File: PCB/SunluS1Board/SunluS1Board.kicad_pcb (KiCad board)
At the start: 2 copper layers, 48.2 x 57 mm, 45 parts, among them J1 Conn_01x14, J2 aNTC, J3 hNTC, J4 Fan, J5 HT, J6 Power, J7 Conn_02x03_Odd_Even, Q1 SIA440DJ-T1-GE3, Q2 AO3400A, Q3 AO3400A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

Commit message: continue routing
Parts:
- moved Q2 0.70 mm to (81.4, 64.4)
- renumbered J4 to FAN, J5 to HT, J6 to Vin, J2 to aNTC, J3 to hNTC
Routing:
- net +24V: track 18.6 -> 56.9 mm
- net Net-(Q2-G): track 0.00 -> 6.04 mm
- net Led: track 0.00 -> 3.97 mm
- net Net-(D1-K): track 0.00 -> 1.95 mm
- net fCon: track 7.49 -> 8.70 mm
- net GND: track 34.6 -> 34.9 mm, vias 7 -> 31
- added copper zone on B.Cu, net GND
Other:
- outline, holes or cut-outs redrawn

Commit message: DRC and 3d models
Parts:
- renumbered aNTC to J2, hNTC to J3, FAN to J4, HT to J5, Vin to J6
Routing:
- net GND: track 34.9 -> 40.4 mm

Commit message: fixes
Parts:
- J7: footprint Connector_PinSocket_2.54mm:PinSocket_2x03_P2.54mm_Vertical_SMD -> Connector_PinHeader_2.54mm:PinHeader_2x03_P2.54mm_Vertical_SMD
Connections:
- J7 pad 1: NRST -> GND
- J7 pad 2: GND -> NRST
- J7 pad 3: SWCLK -> GND
- J7 pad 4: GND -> SWCLK
- J7 pad 5: SWDIO -> +3.3V
- J7 pad 6: +3.3V -> SWDIO
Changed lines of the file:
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@@
 		)
 	)
-	(footprint "Connector_PinSocket_2.54mm:PinSocket_2x03_P2.54mm_Vertical_SMD"
+	(footprint "Connector_PinHeader_2.54mm:PinHeader_2x03_P2.54mm_Vertical_SMD"
 		(layer "F.Cu")
 		(at 93.78 41.36)
-		(descr "surface-mounted straight socket strip, 2x03, 2.54mm pitch, double cols (from Kicad 4.0.7), script generated")
-		(tags "Surface mounted socket strip SMD 2x03 2.54mm double row")
+		(descr "surface-mounted straight pin header, 2x03, 2.54mm pitch, double rows")
+		(tags "Surface mounted pin header SMD 2x03 2.54mm double row")
 		(property "Reference" "J7"
-			(at 0 -5.31 0)
+			(at 0 -4.92 0)
 			(layer "F.SilkS")
 			(effects
@@
 		)
 		(property "Value" "Conn_02x03_Odd_Even"
-			(at 0 5.31 0)
+			(at 0 4.92 0)
 			(layer "F.Fab")
 			(effects
@@
 		(attr smd)
 		(fp_line
-			(start -2.6 -3.87)
-			(end -2.6 -3.3)
+			(start -4.04 -3.35)
+			(end -2.65 -3.35)
 			(stroke
 				(width 0.12)
@@
 		)
 		(fp_line
-			(start -2.6 -3.87)
-			(end 2.6 -3.87)
+			(start -2.65 -3.92)
+			(end -2.65 -3.35)
 			(stroke
 				(width 0.12)
@@
 		)
 		(fp_line
-			(start -2.6 -1.78)
-			(end -2.6 -0.76)
+			(start -2.65 -3.92)
+			(end 2.65 -3.92)
 			(stroke
 				(width 0.12)
@@
 		)
 		(fp_line
-			(start -2.6 0.76)
-			(end -2.6 1.78)
+			(start -2.65 -1.73)
+			(end -2.65 -0.81)
 			(stroke
 				(width 0.12)
@@
 		)
 		(fp_line
-			(start -2.6 3.3)
-			(end -2.6 3.87)
+			(start -2.65 0.81)
+			(end -2.65 1.73)
 			(stroke
 				(width 0.12)
@@
 		)
 		(fp_line
-			(start -2.6 3.87)
-			(end 2.6 3.87)
+			(start -2.65 3.35)
+			(end -2.65 3.92)
 			(stroke
 				(width 0.12)
@@
 		)
 		(fp_line
-			(start 2.6 -3.87)
-			(end 2.6 -3.3)
+			(start -2.65 3.92)
+			(end 2.65 3.92)
 			(stroke
 				(width 0.12)
@@
 		)
 		(fp_line
-			(start 2.6 -3.3)
-			(end 3.96 -3.3)
+			(start 2.65 -3.92)
+			(end 2.65 -3.35)
 			(stroke
 				(width 0.12)
@@
 		)
 		(fp_line
-			(start 2.6 -1.78)
-			(end 2.6 -0.76)
+			(start 2.65 -1.73)
+			(end 2.65 -0.81)
 			(stroke
 				(width 0.12)
@@
 		)
 		(fp_line
-			(start 2.6 0.76)
-			(end 2.6 1.78)
+			(start 2.65 0.81)
+			(end 2.65 1.73)
 			(stroke
 				(width 0.12)
@@
 		)
 		(fp_line
-			(start 2.6 3.3)
-			(end 2.6 3.87)
+			(start 2.65 3.35)
+			(end 2.65 3.92)
 			(stroke
 				(width 0.12)
@@
 		)
 		(fp_line
-			(start -4.55 -4.35)
-			(end 4.5 -4.35)
+			(start -5.87 -4.31)
+			(end -5.87 4.31)
 			(stroke
 				(width 0.05)
@@
 		)
 		(fp_line
-			(start -4.55 4.3)
-			(end -4.55 -4.35)
+			(start -5.87 4.31)
+			(end 5.88 4.31)
 			(stroke
 				(width 0.05)
@@
 		)
 		(fp_line
-			(start 4.5 -4.35)
-			(end 4.5 4.3)
+			(start 5.88 -4.31)
+			(end -5.87 -4.31)
 			(stroke
 				(width 0.05)
@@
 		)
 		(fp_line
-			(start 4.5 4.3)
-			(end -4.55 4.3)
+			(start 5.88 4.31)
+			(end 5.88 -4.31)
 			(stroke
 				(width 0.05)
@@
 		)
 		(fp_line
-			(start -3.92 -2.86)
-			(end -2.54 -2.86)
+			(start -3.6 -2.86)
+			(end -3.6 -2.22)
 			(stroke
 				(width 0.1)
@@
 		)
 		(fp_line
-			(start -3.92 -2.22)
-			(end -3.92 -2.86)
+			(start -3.6 -2.22)
+			(end -2.54 -2.22)
 			(stroke
 				(width 0.1)
@@
 		)
 		(fp_line
-			(start -3.92 -0.32)
-			(end -2.54 -0.32)
+			(start -3.6 -0.32)
+			(end -3.6 0.32)
 			(stroke
 				(width 0.1)
@@
 		)
 		(fp_line
-			(start -3.92 0.32)
-			(end -3.92 -0.32)
+			(start -3.6 0.32)
+			(end -2.54 0.32)
 			(stroke
 				(width 0.1)
@@
 		)
 		(fp_line
-			(start -3.92 2.22)
-			(end -2.54 2.22)
+			(start -3.6 2.22)
+			(end -3.6 2.86)
 			(stroke
 				(width 0.1)
@@
 		)
 		(fp_line
-			(start -3.92 2.86)
-			(end -3.92 2.22)
+			(start -3.6 2.86)
+			(end -2.54 2.86)
 			(stroke
 				(width 0.1)
@@
 		)
 		(fp_line
-			(start -2.54 -3.81)
-			(end 1.54 -3.81)
+			(start -2.54 -2.86)
+			(end -3.6 -2.86)
 			(stroke
 				(width 0.1)
@@
 		)
 		(fp_line
-			(start -2.54 -2.22)
-			(end -3.92 -2.22)
+			(start -2.54 -2.86)
+			(end -1.59 -3.81)
 			(stroke
 				(width 0.1)
@@
 		)
 		(fp_line
-			(start -2.54 0.32)
-			(end -3.92 0.32)
+			(start -2.54 -0.32)
+			(end -3.6 -0.32)
 			(stroke
 				(width 0.1)
@@
 		)
 		(fp_line
-			(start -2.54 2.86)
-			(end -3.92 2.86)
+			(start -2.54 2.22)
+			(end -3.6 2.22)
 			(stroke
 				(width 0.1)
@@
 		(fp_line
 			(start -2.54 3.81)
-			(end -2.54 -3.81)
+			(end -2.54 -2.86)
 			(stroke
 				(width 0.1)
@@
 		)
 		(fp_line
-			(start 1.54 -3.81)
-			(end 2.54 -2.81)
+			(start -1.59 -3.81)
+			(end 2.54 -3.81)
 			(stroke
 				(width 0.1)
@@
 		)
 		(fp_line
-			(start 2.54 -2.86)
-			(end 3.92 -2.86)
+			(start 2.54 -3.81)
+			(end 2.54 3.81)
 			(stroke
 				(width 0.1)
@@
 		)
 		(fp_line
-			(start 2.54 -2.81)
-			(end 2.54 3.81)
+			(start 2.54 -2.86)
+			(end 3.6 -2.86)
 			(stroke
 				(width 0.1)
@@
 		(fp_line
 			(start 2.54 -0.32)
-			(end 3.92 -0.32)
+			(end 3.6 -0.32)
 			(stroke
 				(width 0.1)
@@
 		(fp_line
 			(start 2.54 2.22)
-			(end 3.92 2.22)
+			(end 3.6 2.22)
 			(stroke
 				(width 0.1)
@@
 		)
 		(fp_line
-			(start 3.92 -2.86)
-			(end 3.92 -2.22)
+			(start 3.6 -2.86)
+			(end 3.6 -2.22)
 			(stroke
 				(width 0.1)
@@
 		)
 		(fp_line
-			(start 3.92 -2.22)
+			(start 3.6 -2.22)
 			(end 2.54 -2.22)
 			(stroke
@@
 		)
 		(fp_line
-			(start 3.92 -0.32)
-			(end 3.92 0.32)
+			(start 3.6 -0.32)
+			(end 3.6 0.32)
 			(stroke
 				(width 0.1)
@@
 		)
 		(fp_line
-			(start 3.92 0.32)
+			(start 3.6 0.32)
 			(end 2.54 0.32)
 			(stroke
@@
 		)
 		(fp_line
-			(start 3.92 2.22)
-			(end 3.92 2.86)
+			(start 3.6 2.22)
+			(end 3.6 2.86)
 			(stroke
 				(width 0.1)
@@
 		)
 		(fp_line
-			(start 3.92 2.86)
+			(start 3.6 2.86)
 			(end 2.54 2.86)
 			(stroke
@@
 		)
 		(pad "1" smd rect
-			(at 2.52 -2.54)
-			(size 3 1)
+			(at -2.525 -2.54)
+			(size 3.15 1)
 			(layers "F.Cu" "F.Mask" "F.Paste")
-			(net 22 "NRST")
+			(net 1 "GND")
 			(pinfunction "Pin_1")
 			(pintype "passive")
 		)
 		(pad "2" smd rect
-			(at -2.52 -2.54)
-			(size 3 1)
+			(at 2.525 -2.54)
+			(size 3.15 1)
 			(layers "F.Cu" "F.Mask" "F.Paste")
-			(net 1 "GND")
+			(net 22 "NRST")
 			(pinfunction "Pin_2")
 			(pintype "passive")
 		)
 		(pad "3" smd rect
-			(at 2.52 0)
-			(size 3 1)
+			(at -2.525 0)
+			(size 3.15 1)
 			(layers "F.Cu" "F.Mask" "F.Paste")
-			(net 24 "SWCLK")
+			(net 1 "GND")
 			(pinfunction "Pin_3")
 			(pintype "passive")
 		)
 		(pad "4" smd rect
-			(at -2.52 0)
-			(size 3 1)
+			(at 2.525 0)
+			(size 3.15 1)
 			(layers "F.Cu" "F.Mask" "F.Paste")
-			(net 1 "GND")
+			(net 24 "SWCLK")
 			(pinfunction "Pin_4")
 			(pintype "passive")
 		)
 		(pad "5" smd rect
-			(at 2.52 2.54)
-			(size 3 1)
+			(at -2.525 2.54)
+			(size 3.15 1)
 			(layers "F.Cu" "F.Mask" "F.Paste")
-			(net 23 "SWDIO")
+			(net 4 "+3.3V")
 			(pinfunction "Pin_5")
 			(pintype "passive")
 		)
 		(pad "6" smd rect
-			(at -2.52 2.54)
-			(size 3 1)
+			(at 2.525 2.54)
+			(size 3.15 1)
 			(layers "F.Cu" "F.Mask" "F.Paste")
-			(net 4 "+3.3V")
+			(net 23 "SWDIO")
 			(pinfunction "Pin_6")
 			(pintype "passive")
 		)
 		(embedded_fonts no)
-		(model "${KICAD9_3DMODEL_DIR}/Connector_PinSocket_2.54mm.3dshapes/PinSocket_2x03_P2.54mm_Vertical_SMD.step"
+		(model "${KICAD9_3DMODEL_DIR}/Connector_PinHeader_2.54mm.3dshapes/PinHeader_2x03_P2.54mm_Vertical_SMD.step"
 			(offset
 				(xyz 0 0 0)
@@
 		(at 75.5 68.1)
 		(property "Reference" "SW2"
-			(at 0 4 180)
+			(at 0 -2.9 180)
 			(layer "B.SilkS")
 			(effects
@@
 		(at 97.82 68.1)
 		(property "Reference" "SW1"
-			(at 0 4 180)
+			(at 0 -3.1 180)
 			(layer "B.SilkS")
 			(effects

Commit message: schematic
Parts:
- moved SW2 2.20 mm to (73.3, 68.1)
- moved SW1 2.20 mm to (95.6, 68.1)
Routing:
- net GND: track 40.4 -> 42.8 mm
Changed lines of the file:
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@@
 	(footprint "easyeda2kicad:SW-SMD_L3.9-W3.0-P4.45"
 		(layer "B.Cu")
-		(at 75.5 68.1)
+		(at 73.3 68.1)
 		(property "Reference" "SW2"
 			(at 0 -2.9 180)
@@
 	(footprint "easyeda2kicad:SW-SMD_L3.9-W3.0-P4.45"
 		(layer "B.Cu")
-		(at 97.82 68.1)
+		(at 95.62 68.1)
 		(property "Reference" "SW1"
 			(at 0 -3.1 180)
@@
 	)
 	(via
-		(at 94.4 68.1)
+		(at 95.2 68.1)
 		(size 0.6)
 		(drill 0.3)
@@
 	)
 	(segment
-		(start 95.64 68.1)
-		(end 94.4 68.1)
+		(start 75.401 41.701)
+		(end 79.299 41.701)
+		(width 0.2)
+		(layer "B.Cu")
+		(net 1)
+	)
+	(segment
+		(start 78.5 42.5)
+		(end 78.5 49)
+		(width 0.2)
+		(layer "B.Cu")
+		(net 1)
+	)
+	(segment
+		(start 73.8 47.8)
+		(end 75 49)
+		(width 0.2)
+		(layer "B.Cu")
+		(net 1)
+	)
+	(segment
+		(start 79.299 41.701)
+		(end 79.5 41.5)
+		(width 0.2)
+		(layer "B.Cu")
+		(net 1)
+	)
+	(segment
+		(start 75 49)
+		(end 75.5 49)
+		(width 0.2)
+		(layer "B.Cu")
+		(net 1)
+	)
+	(segment
+		(start 73.32 68.72)
+		(end 71.74 68.72)
+		(width 0.8)
+		(layer "B.Cu")
+		(net 1)
+	)
+	(segment
+		(start 71.74 68.72)
+		(end 71.12 68.1)
+		(width 0.8)
+		(layer "B.Cu")
+		(net 1)
+	)
+	(segment
+		(start 93.44 68.1)
+		(end 95.2 68.1)
 		(width 0.8)
 		(layer "B.Cu")
@@
 	)
 	(segment
-		(start 75.401 41.701)
-		(end 79.299 41.701)
-		(width 0.2)
-		(layer "B.Cu")
-		(net 1)
-	)
-	(segment
-		(start 78.5 42.5)
-		(end 78.5 49)
-		(width 0.2)
-		(layer "B.Cu")
-		(net 1)
-	)
-	(segment
-		(start 73.8 47.8)
-		(end 75 49)
-		(width 0.2)
-		(layer "B.Cu")
-		(net 1)
-	)
-	(segment
-		(start 79.299 41.701)
-		(end 79.5 41.5)
-		(width 0.2)
-		(layer "B.Cu")
-		(net 1)
-	)
-	(segment
-		(start 75 49)
-		(end 75.5 49)
-		(width 0.2)
-		(layer "B.Cu")
-		(net 1)
-	)
-	(segment
 		(start 74 69.4)
 		(end 73.32 68.72)
@@
 		(layer "B.Cu")
 		(net 1)
-	)
-	(segment
-		(start 73.32 68.72)
-		(end 73.32 68.1)
-		(width 0.8)
-		(layer "B.Cu")
-		(net 1)

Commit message: continue buck
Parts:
- removed C5, C7: 100nF, Capacitor_SMD:C_0603_1608Metric
- removed C6, C8: 1uF, Capacitor_SMD:C_0805_2012Metric
- removed D3: 1N4007W, Diode_SMD:Nexperia_CFP3_SOD-123W
- removed U2: AP7381-33SA-7, Package_TO_SOT_SMD:SOT-23
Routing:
- net +24V: track 56.9 -> 48.2 mm
- net +3.3V: track 37.6 -> 34.6 mm, vias 9 -> 7
- net Net-(D3-K): track 2.87 -> 0.00 mm

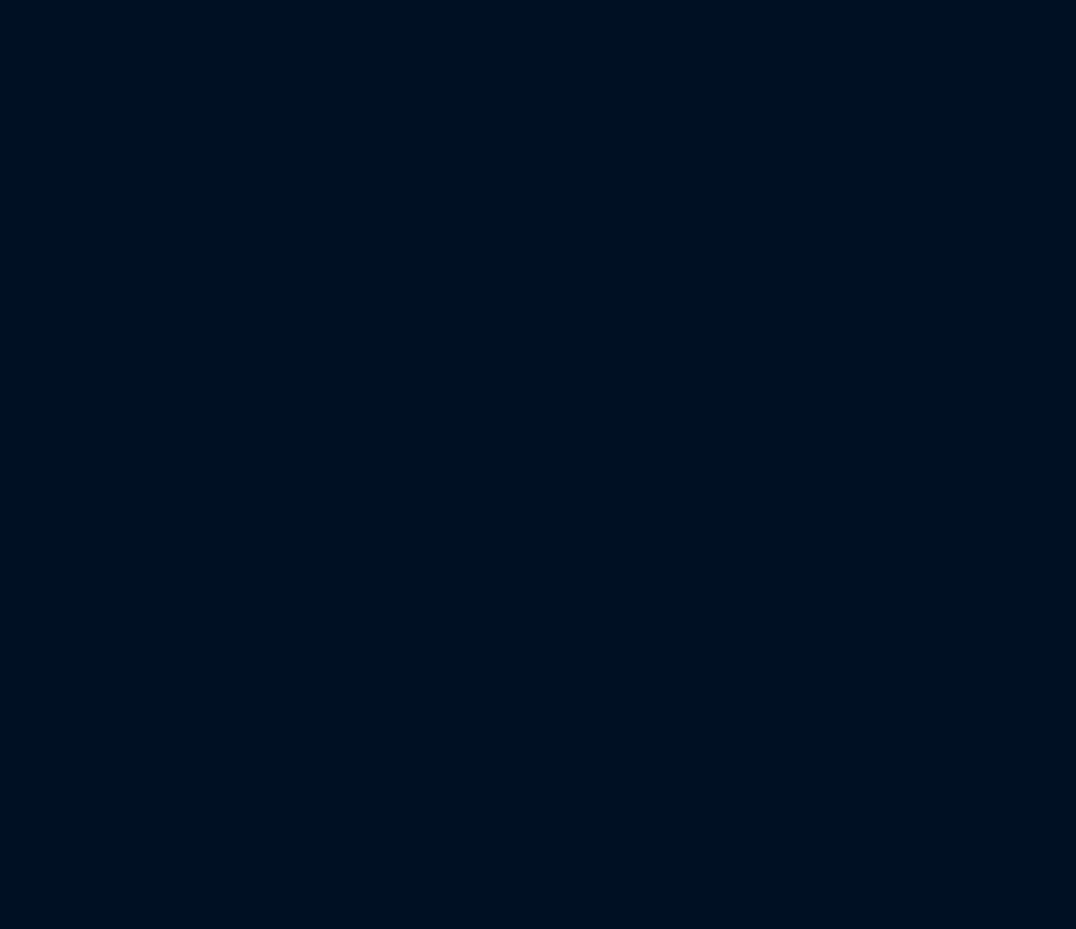
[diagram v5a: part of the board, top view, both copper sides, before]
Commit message: start buck pcb
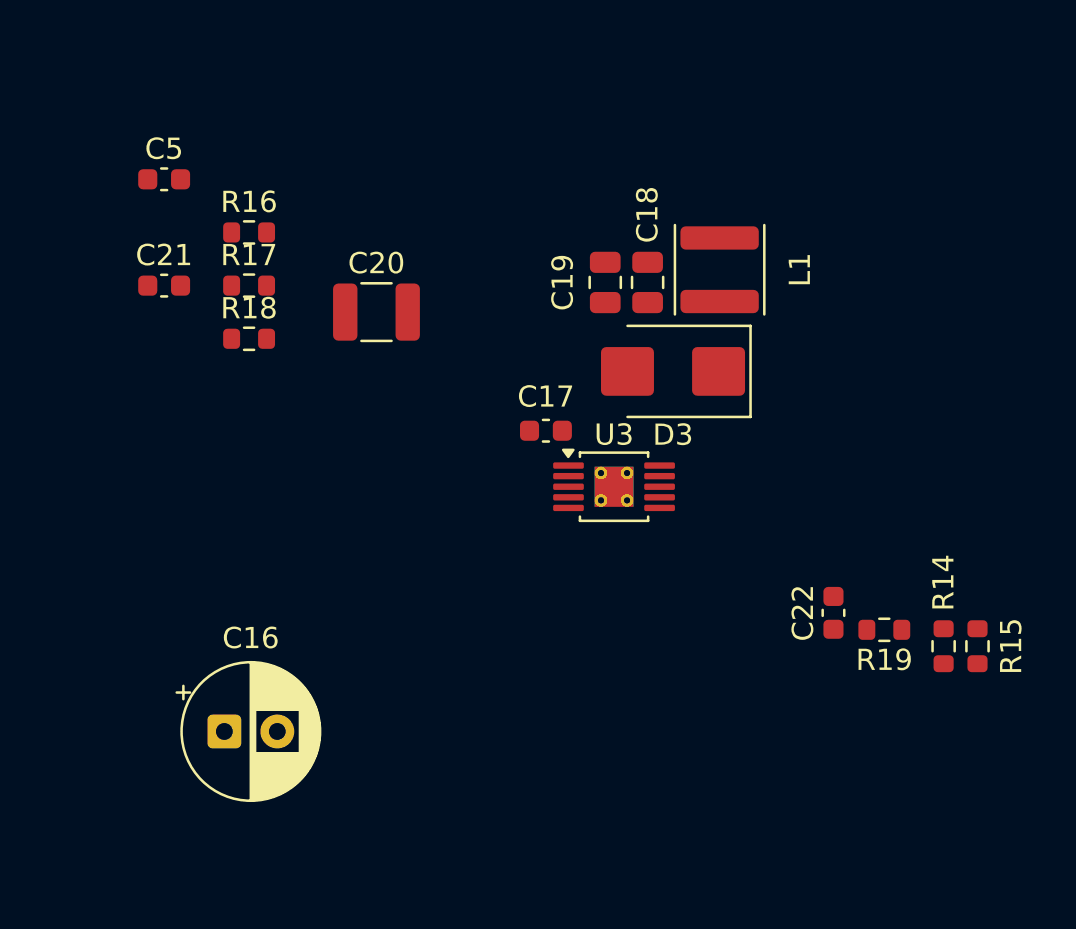
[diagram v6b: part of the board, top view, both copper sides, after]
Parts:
- added C16: 100uF, Capacitor_THT:CP_Radial_D6.3mm_P2.50mm, F.Cu at (125.6, 64.8)
- added C17: 0.1uF, Capacitor_SMD:C_0603_1608Metric, F.Cu at (140.8, 50.6)
- added C18: 22uF, Capacitor_SMD:C_0805_2012Metric, F.Cu at (145.6, 43.6)
- added C19: 22uF, Capacitor_SMD:C_0805_2012Metric, F.Cu at (143.6, 43.6)
- added C20: 10uF, Capacitor_SMD:C_1210_3225Metric, F.Cu at (132.8, 45.0)
- added C21: 10nF, Capacitor_SMD:C_0603_1608Metric, F.Cu at (122.8, 43.8)
- added C22: 4.7nF, Capacitor_SMD:C_0603_1608Metric, F.Cu at (154.4, 59.2)
- added C5: 0.1uF, Capacitor_SMD:C_0603_1608Metric, F.Cu at (122.8, 38.7)
- added D3: B360, Diode_SMD:D_SMB, F.Cu at (146.8, 47.8)
- added L1: 10uH, Inductor_SMD:L_APV_ANR4020, F.Cu at (149.0, 43.0)
- added R14: 31.6k, Resistor_SMD:R_0603_1608Metric, F.Cu at (159.6, 60.8)
- added R15: 10k, Resistor_SMD:R_0603_1608Metric, F.Cu at (161.2, 60.8)
- added R16: 124k, Resistor_SMD:R_0603_1608Metric, F.Cu at (126.8, 41.2)
- added R17: 30.1k, Resistor_SMD:R_0603_1608Metric, F.Cu at (126.8, 43.8)
- added R18: 412k, Resistor_SMD:R_0603_1608Metric, F.Cu at (126.8, 46.3)
- added R19: 20k, Resistor_SMD:R_0603_1608Metric, F.Cu at (156.8, 60.0)
- added U3: TPS54240DGQ, Package_SO:HVSSOP-10-1EP_3x3mm_P0.5mm_EP1.83x1.89mm_ThermalVias, F.Cu at (144.0, 53.2)

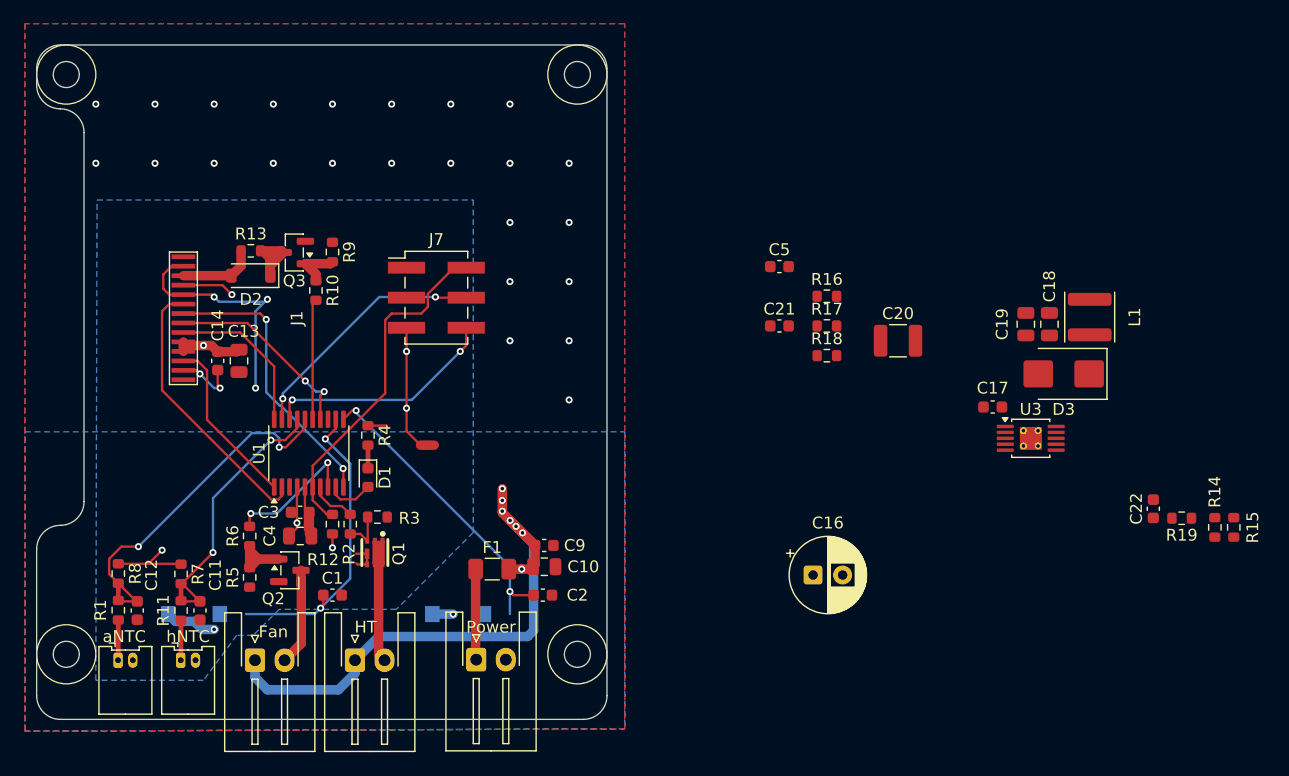
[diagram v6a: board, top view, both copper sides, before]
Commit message: f*** I placed and routed the buck at the wrong layer...
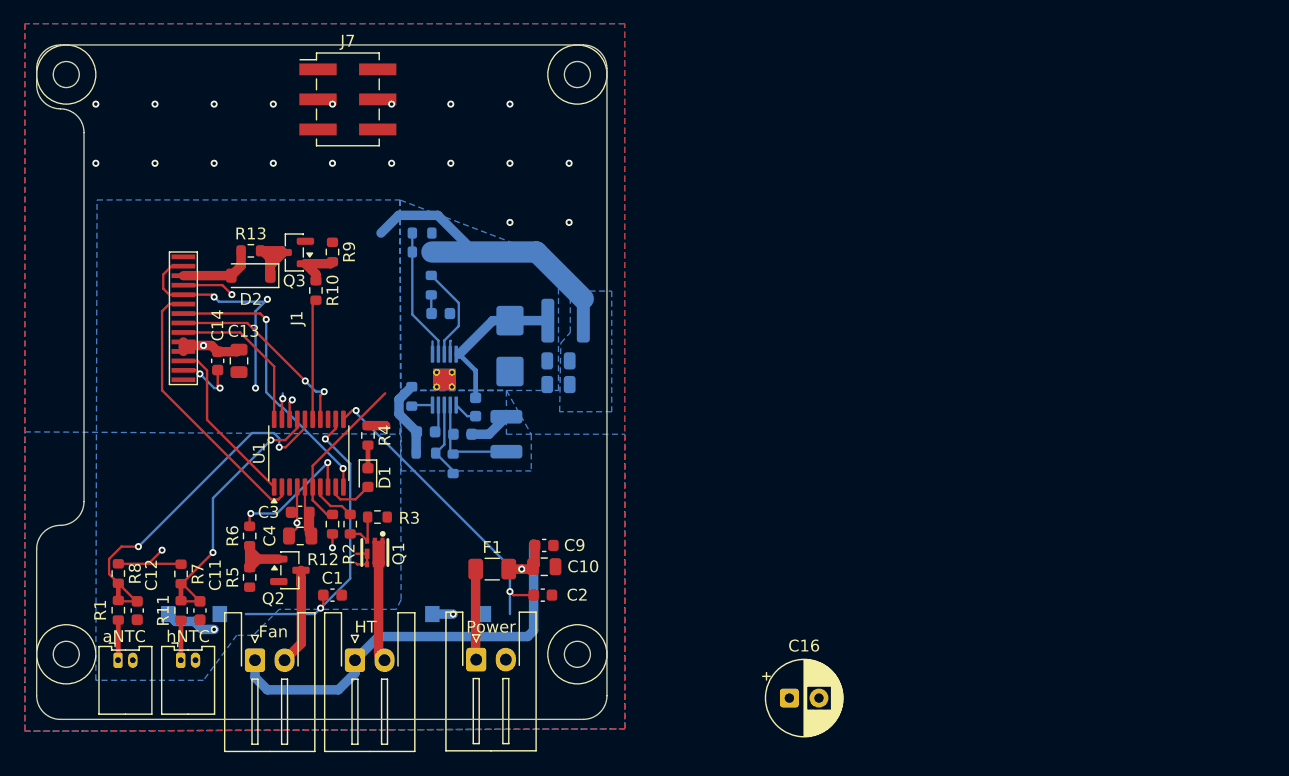
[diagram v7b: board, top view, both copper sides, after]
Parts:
- C17, C18, C19, C20, C21, C22, C5, D3, L1, R14, R15, R16, R17, R18, R19, U3: moved to B.Cu
- moved R15 73.0 mm to (92.6, 35.9), turned to 0 degrees
- moved R14 70.9 mm to (92.6, 37.5), turned to 180 degrees
- moved R19 66.4 mm to (93.3, 40.3), turned to -90 degrees
- moved C22 62.4 mm to (94.2, 42.7), turned to 0 degrees
- moved U3 49.8 mm to (94.5, 48.3), turned to 90 degrees
- moved D3 46.9 mm to (100.0, 45.5), turned to -90 degrees
- moved L1 44.3 mm to (104.7, 43.3), turned to 0 degrees
- moved C17 43.7 mm to (97.1, 50.6), turned to -90 degrees
- moved C18 41.6 mm to (104.1, 46.7), turned to 180 degrees
- moved C19 39.8 mm to (104.1, 48.7), turned to 180 degrees
- moved R17 35.5 mm to (92.9, 54.5), turned to 180 degrees
- moved R18 35.3 mm to (91.7, 49.7), turned to 90 degrees
- moved R16 34.6 mm to (95.2, 55.4), turned to -90 degrees
- moved C20 34.0 mm to (99.7, 52.9), turned to 90 degrees
- moved C21 31.2 mm to (92.9, 52.7), turned to 180 degrees
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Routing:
- net SWCLK: track 21.1 -> 2.22 mm, vias 2 -> 1
- net +3.3V: track 34.6 -> 52.7 mm, vias 7 -> 5
- net SWDIO: track 19.8 -> 1.73 mm, vias 2 -> 1
- net NRST: track 29.3 -> 13.7 mm
- net Net-(D3-K): track 0.00 -> 12.9 mm
- net GND: track 42.8 -> 55.3 mm, vias 31 -> 26
- net Net-(U3-VSENSE): track 0.00 -> 11.1 mm
- net Net-(U3-COMP): track 0.00 -> 8.13 mm
- net Net-(U3-EN): track 0.00 -> 6.70 mm
- net Net-(U3-SS/TR): track 0.00 -> 2.38 mm
- net Net-(U3-BOOT): track 0.00 -> 2.03 mm
- net Net-(U3-RT/CLK): track 0.00 -> 1.79 mm
- net Net-(C22-Pad1): track 0.00 -> 1.59 mm
- net +24V: track 48.2 -> 48.3 mm, vias 7 -> 1
